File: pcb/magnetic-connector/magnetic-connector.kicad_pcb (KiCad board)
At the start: 2 copper layers, 26 x 42 mm, 18 parts

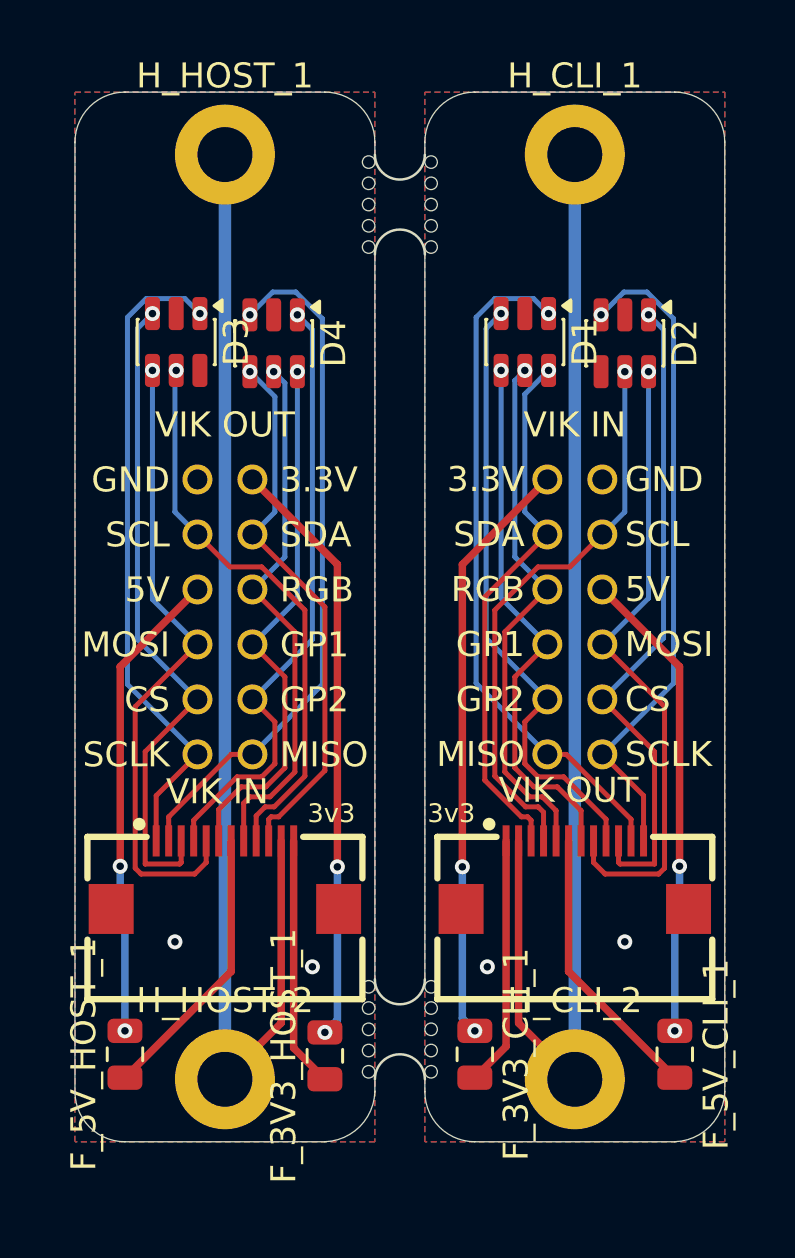
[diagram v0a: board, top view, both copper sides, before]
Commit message: Change ESD protection chips on magnetic connector.
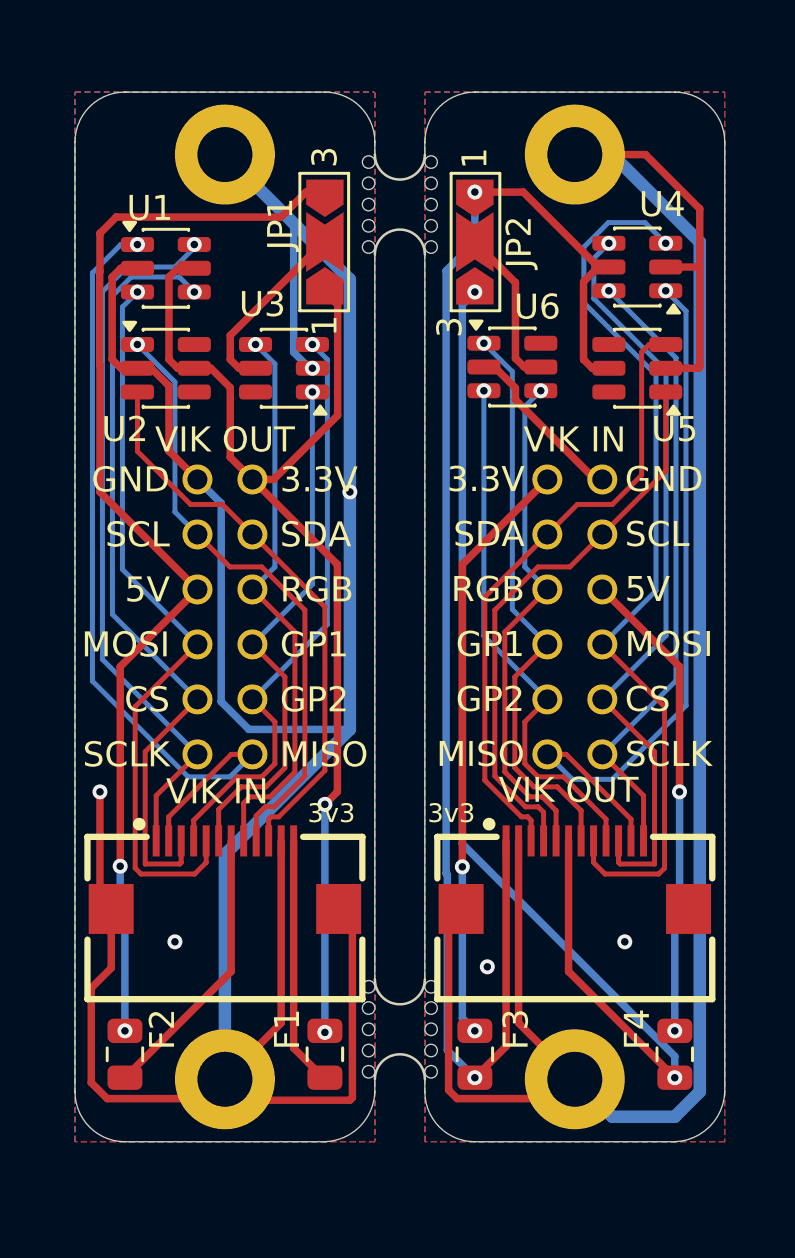
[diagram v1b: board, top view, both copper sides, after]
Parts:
- removed D1, D2, D3, D4: ESDA6V1-5SC6, Package_TO_SOT_SMD:SOT-23-6
- added JP1: SolderJumper_3_Open, Jumper:SolderJumper-3_P2.0mm_Open_TrianglePad1.0x1.5mm_NumberLabels, F.Cu at (30.0, 26.0)
- added JP2: SolderJumper_3_Open, Jumper:SolderJumper-3_P2.0mm_Open_TrianglePad1.0x1.5mm_NumberLabels, F.Cu at (36.0, 26.0)
- added U1: CLAMP0504DT, Package_TO_SOT_SMD:SOT-23-6, F.Cu at (23.6, 27.1)
- added U2: CLAMP0504DT, Package_TO_SOT_SMD:SOT-23-6, F.Cu at (23.6, 31.1)
- added U3: CLAMP0504DT, Package_TO_SOT_SMD:SOT-23-6, F.Cu at (28.4, 31.1)
- added U4: CLAMP0504DT, Package_TO_SOT_SMD:SOT-23-6, F.Cu at (42.5, 27.0)
- added U5: CLAMP0504DT, Package_TO_SOT_SMD:SOT-23-6, F.Cu at (42.5, 31.1)
- added U6: CLAMP0504DT, Package_TO_SOT_SMD:SOT-23-6, F.Cu at (37.5, 31.0)
- moved F2 8.00 mm to (22.0, 58.5)
- moved F1 8.00 mm to (30.0, 58.5)
- renumbered F_5V_HOST_1 to F1, F_3V3_HOST_1 to F2, F_3V3_CLI_1 to F3, F_5V_CLI_1 to F4
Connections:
- F1 pad 1: /Host/5V_IN -> /Host/3V3_IN
- F1 pad 2: /Host/5V_OUT -> /Host/3V3_OUT
- F2 pad 1: /Host/3V3_IN -> /Host/5V_IN
- F2 pad 2: /Host/3V3_OUT -> /Host/5V_OUT
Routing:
- net /Host/GND: track 47.5 -> 119.3 mm, vias 2 -> 4
- net /Client/3V3_OUT: track 10.0 -> 58.1 mm, vias 0 -> 2
- net /Client/GND: track 47.5 -> 91.8 mm
- net /Client/5V_OUT: track 11.2 -> 46.4 mm, vias 0 -> 2
- net /Host/5V_OUT: track 19.0 -> 44.6 mm
- net /Host/3V3_OUT: track 23.7 -> 44.8 mm
- net /Client/MOSI: track 25.7 -> 36.0 mm
- net Net-(JP1-C): track 0.00 -> 7.45 mm
- net Net-(JP2-C): track 0.00 -> 6.48 mm
- net /Host/CS: track 26.5 -> 31.2 mm
- net /Host/MISO: track 27.7 -> 32.3 mm
- net /Client/CS: track 26.4 -> 30.5 mm
- net /Host/MOSI: track 25.7 -> 29.6 mm
- net /Client/SDA: track 21.5 -> 25.0 mm, vias 1 -> 0
- net /Client/GP2: track 24.7 -> 21.4 mm
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
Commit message: Increase hole size on magnetic connector PCB.
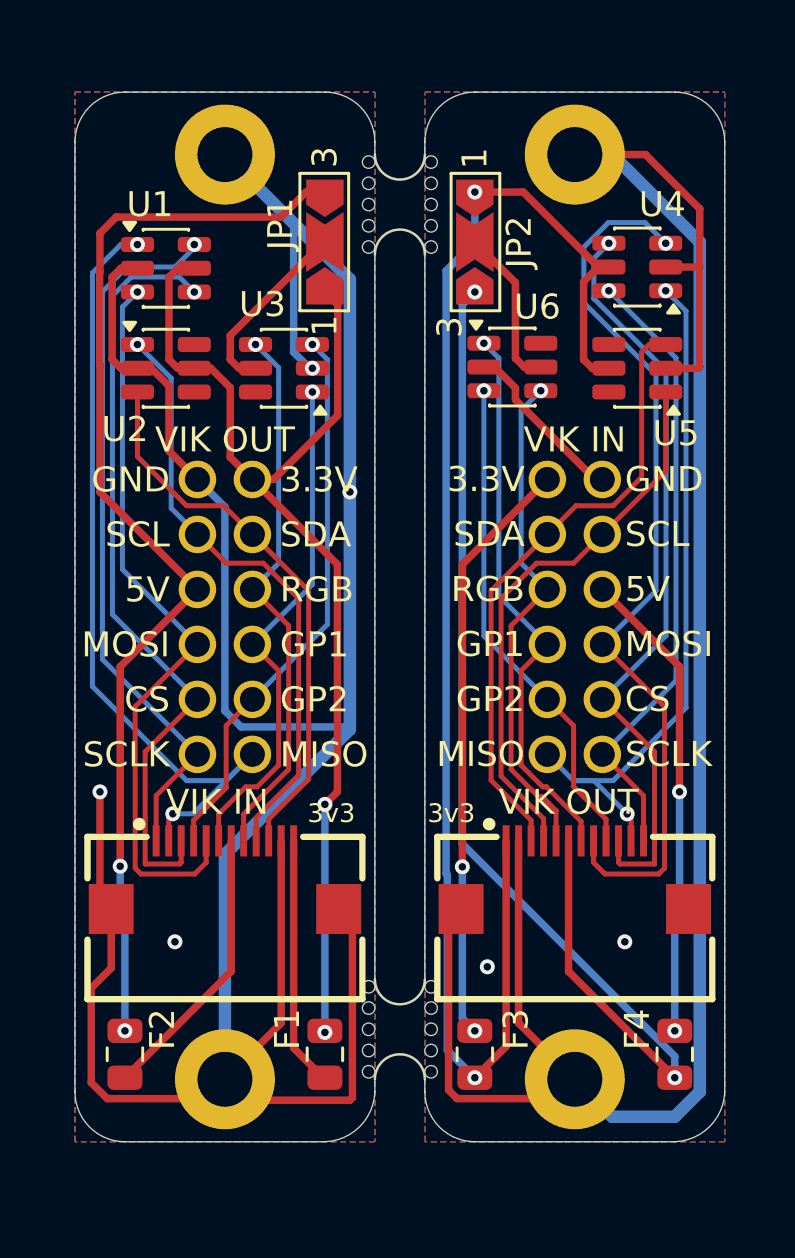
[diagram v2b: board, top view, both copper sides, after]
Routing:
- net /Client/MISO: track 29.4 -> 28.1 mm, vias 1 -> 2
- net /Client/GP2: track 21.4 -> 20.0 mm
- net /Host/GP2: track 23.6 -> 22.3 mm
- net /Client/GP1: track 23.1 -> 22.5 mm
- net /Host/SDA: track 22.9 -> 22.3 mm
- net /Host/RGB_DO: track 22.6 -> 22.0 mm
- net /Host/GP1: track 21.2 -> 20.6 mm
- net /Host/MISO: track 32.3 -> 32.5 mm, vias 1 -> 2
